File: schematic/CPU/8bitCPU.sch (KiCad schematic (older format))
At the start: 1 part, among them U29 74LS08

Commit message: schematic finished
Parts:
- added C10, C11: 0.1uF, symbol Device:C_Small
- added D56: bus7, LED_THT:LED_D3.0mm, symbol Device:LED
- added D57: bus6, LED_THT:LED_D3.0mm, symbol Device:LED
- added D58: bus5, LED_THT:LED_D3.0mm, symbol Device:LED
- added D59: bus4, LED_THT:LED_D3.0mm, symbol Device:LED
- added D60: bus3, LED_THT:LED_D3.0mm, symbol Device:LED
- added D61: bus2, LED_THT:LED_D3.0mm, symbol Device:LED
- added D62: bus1, LED_THT:LED_D3.0mm, symbol Device:LED
- added D63: bus0, LED_THT:LED_D3.0mm, symbol Device:LED
- added R100, R101, R102, R95, R96, R97, R98, R99: 1k, symbol Device:R
- added R103, R104, R105, R106, R107, R108, R109, R110: 1k, Resistor_THT:R_Axial_DIN0207_L6.3mm_D2.5mm_P7.62mm_Horizontal, symbol Device:R
- added U77: 74LS245, symbol 74xx:74LS245
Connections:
- net +5V: now also R100.1, R101.1, R102.1, R95.1, R96.1, R97.1, R98.1, R99.1, U77.1 (A->B), U77.20 (VCC)
- net GND: now also C10.2, C11.2, D56.1 (K), D57.1 (K), D58.1 (K), D59.1 (K), D60.1 (K), D61.1 (K), D62.1 (K), D63.1 (K), U77.10 (GND), U77.19 (CE)
- net bus0: now also R102.2, U77.9 (A7)
- net bus1: now also R101.2, U77.8 (A6)
- net bus2: now also R100.2, U77.7 (A5)
- net bus3: now also R99.2, U77.6 (A4)
- net bus4: now also R98.2, U77.5 (A3)
- net bus5: now also R97.2, U77.4 (A2)
- net bus6: now also R96.2, U77.3 (A1)
- net bus7: now also R95.2, U77.2 (A0)
- net ctrlReg0WE: now also C10.1
- net ctrlReg1WE: now also C11.1
- new net: R110.2, U77.11 (B7)
- new net: R109.2, U77.12 (B6)
- new net: R108.2, U77.13 (B5)
- new net: R107.2, U77.14 (B4)
- new net: R106.2, U77.15 (B3)
- new net: R105.2, U77.16 (B2)
- new net: R104.2, U77.17 (B1)
- new net: R103.2, U77.18 (B0)
- new net: D56.2 (A), R103.1
- new net: D57.2 (A), R104.1
- new net: D58.2 (A), R105.1
- new net: D59.2 (A), R106.1
- new net: D60.2 (A), R107.1
- new net: D61.2 (A), R108.1
- new net: D62.2 (A), R109.1
- new net: D63.2 (A), R110.1
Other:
- note added: "+1 74ls374 of board 03"
- note added: "00 is top left\n01 is top right\n06 is bottom left\n16 is bottom right\n"
- note added: "Board Layout Numbering:"
- note added: "board 00/01/10/11/12"
- note added: "board 02/03"
- note added: "board 03"
- note added: "board 04/14"
- note added: "board 05/15"
- note added: "board 06"
- note added: "board 13"
- note added: "board 16"
- moved on the sheet: U29A, U29B, U29C, U29D, U29E

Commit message: updated schematic
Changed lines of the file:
@@
 F8 "b6" I L 12600 5050 50
 F9 "b7" I L 12600 5150 50
-F11 "halt" O L 12600 5300 50
+F10 "halt" O L 12600 5300 50
 $EndSheet
 Text Label 11700 4900 2    50   ~ 0
@@
 	2300 2100 13100 2100
 Wire Notes Line width 12
-	11300 7350 11300 2100
-Wire Notes Line width 12
 	12550 6050 12550 7600
 Wire Notes Line width 12
 	13700 3900 13700 6050
-Wire Notes Line width 12
-	13700 6050 12550 6050
 Text Notes 11350 4100 0    100  ~ 20
 board 04/14
@@
 	11300 3900 13700 3900
 Wire Notes Line width 12
-	11300 6050 12550 6050
-Wire Notes Line width 12
 	12550 7600 11300 7600
-Wire Notes Line width 12
-	11300 7600 11300 7350
 Text Notes 11350 4200 0    50   ~ 10
 +1 74ls374 of board 03
+Wire Notes Line width 12
+	11300 2100 11300 7600
+Wire Notes Line width 12
+	11300 6050 13700 6050
 $EndSCHEMATC

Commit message: pre upgrade to vivado 2021
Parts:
- removed C10, C11: 0.1uF, symbol Device:C_Small
- removed U29: 74LS08, Package_DIP:DIP-14_W7.62mm, symbol 74xx:74LS08
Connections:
- no-connect marks 3 -> 0
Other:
- note removed: "+1 74ls374 of board 03"
- note removed: "00 is top left\n01 is top right\n06 is bottom left\n16 is bottom right\n"
- note removed: "Board Layout Numbering:"
- note removed: "board 00/01/10/11/12"
- note removed: "board 02/03"
- note removed: "board 03"
- note removed: "board 04/14"
- note removed: "board 05/15"
- note removed: "board 06"
- note removed: "board 13"
- note removed: "board 16"

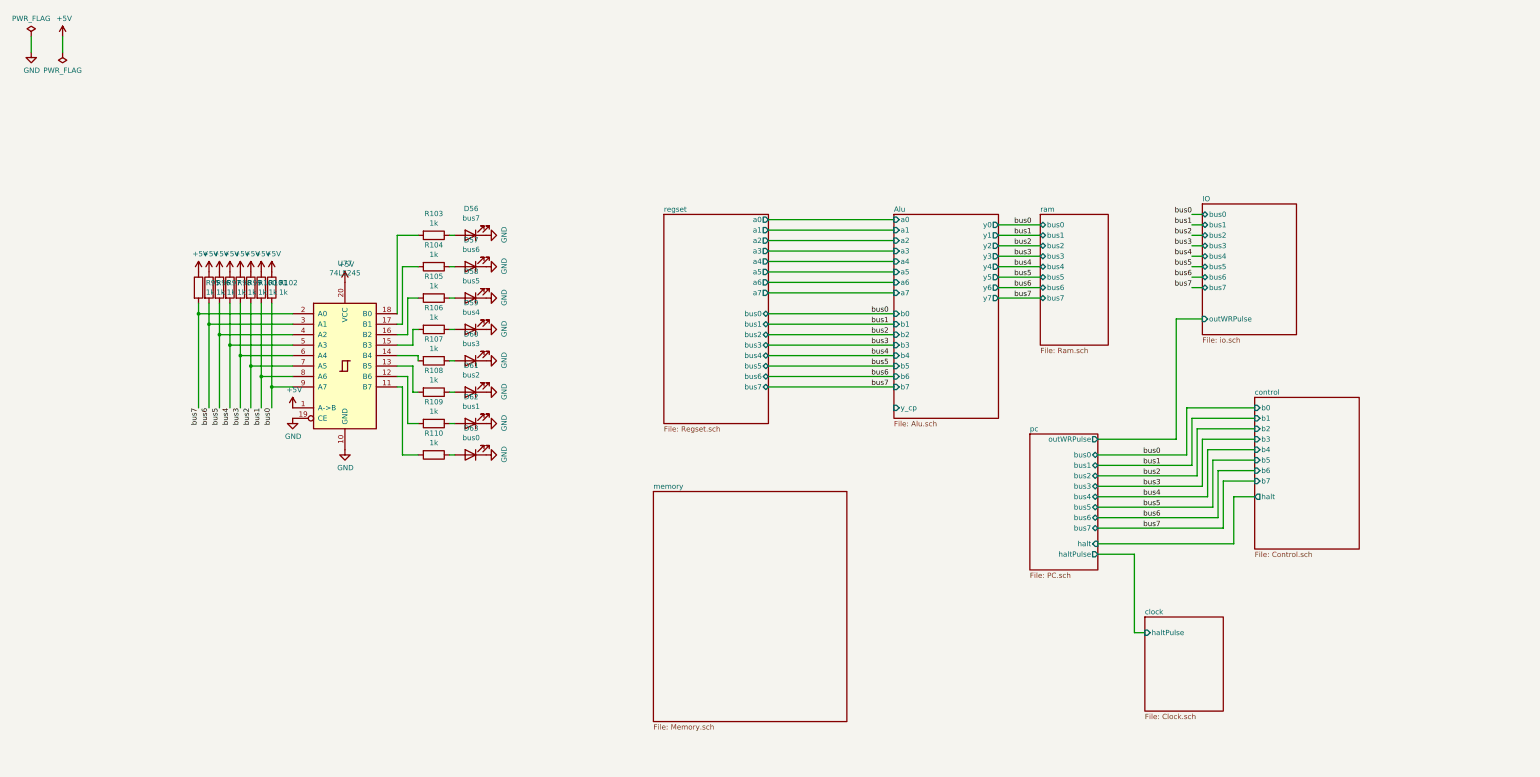
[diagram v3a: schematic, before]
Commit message: fibonacci works again with new memory design
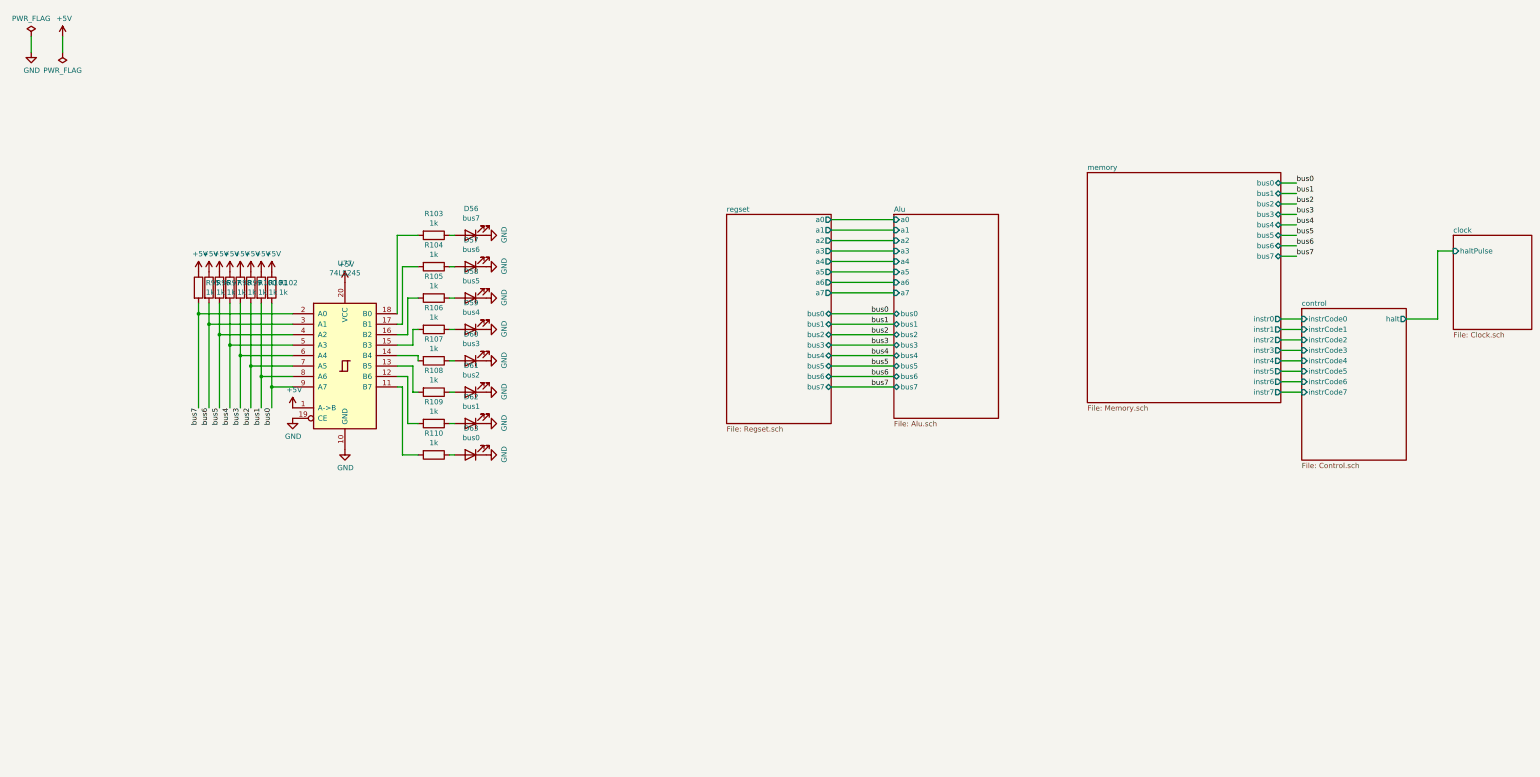
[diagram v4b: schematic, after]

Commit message: schematic with henry
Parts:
- removed D56: bus7, LED_THT:LED_D3.0mm, symbol Device:LED
- removed D57: bus6, LED_THT:LED_D3.0mm, symbol Device:LED
- removed D58: bus5, LED_THT:LED_D3.0mm, symbol Device:LED
- removed D59: bus4, LED_THT:LED_D3.0mm, symbol Device:LED
- removed D60: bus3, LED_THT:LED_D3.0mm, symbol Device:LED
- removed D61: bus2, LED_THT:LED_D3.0mm, symbol Device:LED
- removed D62: bus1, LED_THT:LED_D3.0mm, symbol Device:LED
- removed D63: bus0, LED_THT:LED_D3.0mm, symbol Device:LED
- removed R100, R101, R102, R95, R96, R97, R98, R99: 1k, symbol Device:R
- removed R103, R104, R105, R106, R107, R108, R109, R110: 1k, Resistor_THT:R_Axial_DIN0207_L6.3mm_D2.5mm_P7.62mm_Horizontal, symbol Device:R
- removed U77: 74LS245, symbol 74xx:74LS245
- added D1, D2, D3, D4, D5, D6, D7, D8: LED_Small, symbol Device:LED_Small
- added RN1: 10k, Resistor_THT:R_Array_SIP9, symbol Device:R_Network08
- added RN2: 220, Resistor_THT:R_Array_SIP9, symbol Device:R_Network08
- added U1: 74ABT540, symbol 8bitCPU-rescue:74ABT540
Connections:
- net +5V: now also RN1.1 (common), RN2.1 (common), U1.20 (VCC)
- net GND: now also U1.1 (~OE1~), U1.10 (GND), U1.19 (~OE2~)
- net bus0: now also RN1.2 (R1), U1.2 (A0)
- net bus1: now also RN1.3 (R2), U1.3 (A1)
- net bus2: now also RN1.4 (R3), U1.4 (A2)
- net bus3: now also RN1.5 (R4), U1.5 (A3)
- net bus4: now also RN1.6 (R5), U1.6 (A4)
- net bus5: now also RN1.7 (R6), U1.7 (A5)
- net bus6: now also RN1.8 (R7), U1.8 (A6)
- net bus7: now also RN1.9 (R8), U1.9 (A7)
- new net: D8.1 (K), U1.11 (Y7)
- new net: D7.1 (K), U1.12 (Y6)
- new net: D6.1 (K), U1.13 (Y5)
- new net: D5.1 (K), U1.14 (Y4)
- new net: D4.1 (K), U1.15 (Y3)
- new net: D3.1 (K), U1.16 (Y2)
- new net: D2.1 (K), U1.17 (Y1)
- new net: D1.1 (K), U1.18 (Y0)
- new net: D1.2 (A), RN2.2 (R1)
- new net: D2.2 (A), RN2.3 (R2)
- new net: D3.2 (A), RN2.4 (R3)
- new net: D4.2 (A), RN2.5 (R4)
- new net: D5.2 (A), RN2.6 (R5)
- new net: D6.2 (A), RN2.7 (R6)
- new net: D7.2 (A), RN2.8 (R7)
- new net: D8.2 (A), RN2.9 (R8)
